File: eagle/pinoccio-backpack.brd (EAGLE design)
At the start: 25.4 x 42.7 mm, 5 parts, among them J1 AVR_SPI_PRG_6

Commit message: Version 1.0
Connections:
- removed net N$2: J1.1, U$3.7
- new net N$1: J1.4, U$3.6
- net BKPK-BUS: now also J1.1, U$3.7; no longer J1.4, U$3.6
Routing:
- net N$1: track 0.00 -> 6.92 mm, vias 0 -> 1
- net BKPK-BUS: track 17.5 -> 12.0 mm
- net N$2: track 3.72 -> 0.00 mm, vias 1 -> 0
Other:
- board text added: "2013-07-01"
- board text added: "Pinoccio(tm) Backpack Reference v1.0"
- board text added: "VBAT"
- board text added: "reference backpack v0.1"
- board text removed: "BAT"
- board text removed: "Pinoccio(tm) Backpack Reference v0.13"

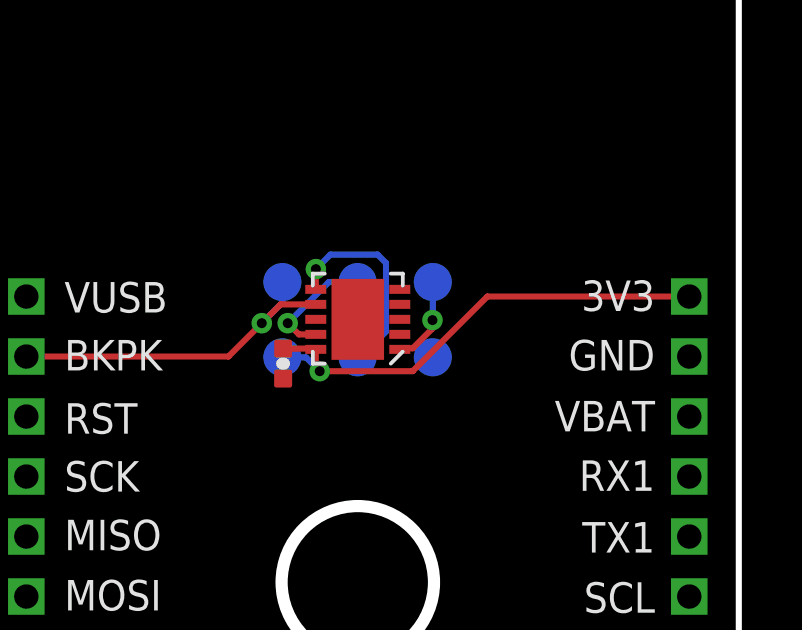
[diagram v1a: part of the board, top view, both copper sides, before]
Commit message: Added reset pull-up to tiny13
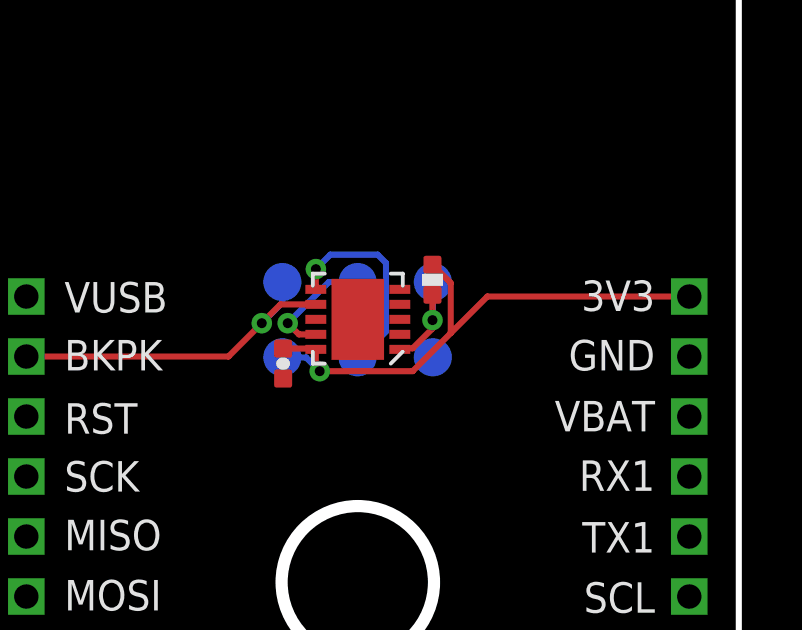
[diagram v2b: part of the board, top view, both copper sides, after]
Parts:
- added R1: 100K, Pinoccio:0402-RES
- renumbered U$3 to U1
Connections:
- net N$4: now also R1.1
- net VCC-AE: now also R1.2
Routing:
- net VCC-AE: track 16.7 -> 19.2 mm
- net N$4: track 2.93 -> 3.78 mm
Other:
- board text added: "2013-08-15"
- board text added: "reference backpack v1.0"
- board text removed: "2013-07-01"
- board text removed: "reference backpack v0.1"
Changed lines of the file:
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@@
 <text x="14.986" y="41.4528" size="0.8128" layer="22" ratio="15" rot="MR0">tiny13A</text>
 <circle x="12.7" y="29.845" radius="2.54" width="0.4064" layer="20"/>
-<text x="20.828" y="49.3268" size="0.8128" layer="22" ratio="15" rot="MR0">reference backpack v0.1</text>
-<text x="16.256" y="47.9552" size="0.8128" layer="22" ratio="15" rot="MR0">2013-07-01</text>
+<text x="20.828" y="49.3268" size="0.8128" layer="22" ratio="15" rot="MR0">reference backpack v1.0</text>
+<text x="16.256" y="47.9552" size="0.8128" layer="22" ratio="15" rot="MR0">2013-08-15</text>
 </plain>
 <attributes>
@@
 <element name="JP-R" library="Pinoccio" package="1X16_2MM" value="M162MM" x="23.749" y="39.37" locked="yes" smashed="yes" rot="R270"/>
 <element name="JP-L" library="Pinoccio" package="1X16_2MM" value="M162MM" x="1.651" y="39.37" locked="yes" smashed="yes" rot="R270"/>
-<element name="U$3" library="Pinoccio" package="QFN-10" value="ATTINY13QFN10" x="12.7" y="38.608" rot="R180"/>
+<element name="U1" library="Pinoccio" package="QFN-10" value="ATTINY13QFN10" x="12.7" y="38.608" rot="R180"/>
 <element name="J1" library="Pinoccio" package="2X3-PAD" value="AVR_SPI_PRG_6" x="10.1854" y="39.8526" locked="yes" rot="MR180"/>
 <element name="C7" library="Pinoccio" package="0402-CAP" value="0.1uf" x="10.2108" y="37.1348" smashed="yes" rot="R270"/>
+<element name="R1" library="Pinoccio" package="0402-RES" value="100K" x="15.1892" y="39.9288" smashed="yes" rot="R90"/>
 </elements>
 <signals>
@@
 <vertex x="0.1016" y="50.8762"/>
 </polygon>
-<contactref element="U$3" pad="EP"/>
-<contactref element="U$3" pad="5"/>
+<contactref element="U1" pad="EP"/>
+<contactref element="U1" pad="5"/>
 <contactref element="C7" pad="2"/>
 <contactref element="J1" pad="6"/>
@@
 <signal name="VCC-AE">
 <contactref element="JP-R" pad="P$1"/>
-<contactref element="U$3" pad="10"/>
+<contactref element="U1" pad="10"/>
 <contactref element="C7" pad="1"/>
 <contactref element="J1" pad="2"/>
@@
 <wire x1="11.2252" y1="37.6348" x2="10.2108" y2="37.6348" width="0.2032" layer="1"/>
 <wire x1="23.749" y1="39.37" x2="17.018" y2="39.37" width="0.2032" layer="1"/>
-<wire x1="17.018" y1="39.37" x2="14.5288" y2="36.8808" width="0.2032" layer="1"/>
+<wire x1="17.018" y1="39.37" x2="15.7988" y2="38.1508" width="0.2032" layer="1"/>
+<wire x1="15.7988" y1="38.1508" x2="14.5288" y2="36.8808" width="0.2032" layer="1"/>
 <wire x1="14.5288" y1="36.8808" x2="11.43" y2="36.8808" width="0.2032" layer="1"/>
+<contactref element="R1" pad="2"/>
+<wire x1="15.1892" y1="40.4288" x2="15.7988" y2="39.8192" width="0.2032" layer="1"/>
+<wire x1="15.7988" y1="39.8192" x2="15.7988" y2="38.1508" width="0.2032" layer="1"/>
 </signal>
 <signal name="VIN">
@@
 <contactref element="JP-L" pad="P$2"/>
 <contactref element="J1" pad="1"/>
-<contactref element="U$3" pad="7"/>
+<contactref element="U1" pad="7"/>
 <wire x1="11.3" y1="39.108" x2="10.1266" y2="39.108" width="0.2032" layer="1"/>
 <wire x1="10.1266" y1="39.108" x2="9.4996" y2="38.481" width="0.2032" layer="1"/>
@@
 <signal name="N$3">
 <contactref element="J1" pad="3"/>
-<contactref element="U$3" pad="9"/>
+<contactref element="U1" pad="9"/>
 <wire x1="11.3" y1="38.108" x2="10.7362" y2="38.108" width="0.2032" layer="1"/>
 <wire x1="10.7362" y1="38.108" x2="10.3632" y2="38.481" width="0.2032" layer="1"/>
@@
 <signal name="N$4">
 <contactref element="J1" pad="5"/>
-<contactref element="U$3" pad="1"/>
+<contactref element="U1" pad="1"/>
 <wire x1="14.1" y1="37.608" x2="14.1348" y2="37.6428" width="0.2032" layer="1"/>
 <wire x1="14.1348" y1="37.6428" x2="14.5288" y2="37.6428" width="0.2032" layer="1"/>
@@
 <wire x1="15.1892" y1="38.5826" x2="15.2014" y2="38.5948" width="0.2032" layer="16"/>
 <wire x1="15.2014" y1="38.5948" x2="15.2014" y2="39.8526" width="0.2032" layer="16"/>
+<contactref element="R1" pad="1"/>
+<wire x1="15.1892" y1="39.4288" x2="15.1892" y2="38.5826" width="0.2032" layer="1"/>
 </signal>
 <signal name="N$1">
@@
 <wire x1="12.7828" y1="37.3446" x2="12.6934" y2="37.3446" width="0.2032" layer="16"/>
 <wire x1="11.303" y1="40.2844" x2="11.3" y2="40.2814" width="0.2032" layer="1"/>
-<contactref element="U$3" pad="6"/>
+<contactref element="U1" pad="6"/>
 <wire x1="11.3" y1="39.608" x2="11.303" y2="39.608" width="0.2032" layer="1"/>
 <wire x1="11.303" y1="39.608" x2="11.303" y2="40.2844" width="0.2032" layer="1"/>
